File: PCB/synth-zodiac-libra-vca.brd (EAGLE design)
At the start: 160 x 100 mm, 29 parts, among them J4 6.35MM JACK, Q8 PNP, U2 LM13700

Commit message: Snapshot of designs so far.
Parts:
- removed C33: 2.2uF/16V, rlc:CAP_ALUM_SMT_4
- removed C34, C35: 0.1uF, rlc:0603-CAP
- removed J4: 6.35MM JACK, con-trs:TE-CK-6.35-29B
- removed JMP1, JMP2, JMP3, JMP4, JMP5, JMP6, JMP7: NP, rlc:0603-RES
- removed JMP62: 0, rlc:0603-RES
- removed R46, R48: 681R, rlc:0603-RES
- removed R47: 33.2K, rlc:0603-RES
- removed R49: 4.99K, rlc:0603-RES
- removed R50, R54, R55: 10.0K, rlc:0603-RES
- removed R51: 12.1K, rlc:0603-RES
- removed R52: 475R, rlc:0603-RES
- removed R53: 4.75M, rlc:0603-RES
- removed R56: 499K, rlc:0603-RES
- removed U2: LM13700, op-amp:SO16
- removed VCF_OUT: TPTHD-038, con-testpoints:THD-038MIL-X1
- added +, -, A.OUT, A_BIAS, BUF.I, BUF.O, D_BIAS: PADSMD-050X050, con-testpoints:SMD-050X050
- added AUD_OUT_TS, TP_COW_IN, TP_VCF_IN: TPSMD-040-RND, con-testpoints:SMD-040MIL-RND
- added A_OUT, COW_IN, EG_IN, VCF_IN: 2-pin, VT, SMT, con-jst:B2B-PH-SM4
- added C1: 2.2uF/16V, rlc:CAP_ALUM_SMT_4
- added C2, C3: 0.1uF, rlc:0603-CAP
- added CONST: Libra, circuit-monkey-zodiac:LIBRA-CONST
- added GLYPH: Libra, circuit-monkey-zodiac:LIBRA-GLYPH
- added J1: (no value), con-jst:B4B-PH-SM4
- added JMP8: NP, rlc:0603-SHORT
- added MODE: SPDT, switch-thd:SS-12-F45-PNL-SMT
- added OUT: 6.35MM JACK, con-trs:PNL-6.35-SMT-PADS
- added PCB: PCB FAB, circuit-monkey-zodiac:PENTAGON-40MM-RAD
- added R1, R10, R2, R3, R4: 10.0K, rlc:0603-RES
- added R11: 4.75M, rlc:0603-RES
- added R12: 4.99K, rlc:0603-RES
- added R13: 12.1K, rlc:0603-RES
- added R14: 475R, rlc:0603-RES
- added R5: 22.1K, rlc:0603-RES
- added R6: 499K, rlc:0603-RES
- added R7: 33.2K, rlc:0603-RES
- added R8, R9: 681R, rlc:0603-RES
- added U1: LM13700, op-amp:SO16
- AUD_OUT, TP1: value TPTHD-038 -> TPSMD-040-RND; device con-testpoints:THD-038MIL-X1 -> con-testpoints:SMD-040MIL-RND
- GND_VCA: value TPTHD-SCOPE-LOOP -> TPSMD-040-RND; device con-testpoints:TP-2P-THD -> con-testpoints:SMD-040MIL-RND
- moved TP1 111.3 mm to (33.4, 43.2), flipped to the bottom
- moved Q8 95.5 mm to (31.9, 47.5), flipped to the bottom, turned to 90 degrees
- moved GND_VCA 82.6 mm to (17.6, 41.6), flipped to the bottom, turned to 180 degrees
- moved AUD_OUT 79.3 mm to (23.7, 34.1), flipped to the bottom, turned to 180 degrees
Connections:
- removed net N$71: JMP5.1, U2.5
- removed net N$72: JMP2.2, U2.2
- removed net N$74: JMP6.2, U2.7
- removed net N$75: JMP7.1, U2.8
- new net AUDIO_OUT_TS: AUD_OUT_TS.TP, A_OUT.1, OUT.TS
- new net COWBELL_IN: COW_IN.1, R2.1, TP_COW_IN.TP
- new net EG_VCA: EG_IN.1, MODE.A
- new net N$1: D_BIAS.1, U1.2
- new net N$142: MODE.B, R5.1
- new net N$2: A.OUT.1, U1.5
- new net N$3: BUF.I.1, U1.7
- new net N$4: BUF.O.1, U1.8
- new net VCF_IN: R1.1, TP_VCF_IN.TP, VCF_IN.1
- net +9V: now also C2.2, J1.1, R5.2, U1.11; no longer C34.2, U2.11
- net -9V: now also C3.1, J1.2, R11.1, R13.1, R6.1, U1.6; no longer C35.1, R53.1, R56.1, U2.6
- net AUDIO_OUT: now also AUD_OUT.TP, OUT.T, R14.2; no longer AUD_OUT.1, J4.T, R52.2
- net EXP_VCA_CV: now also R4.1, R6.2; no longer R55.1, R56.2
- net GND: now also A_OUT.2, C2.1, C3.2, COW_IN.2, EG_IN.2, GND_VCA.TP, J1.4, MODE.MTG1, MODE.MTG2, OUT.S, OUT.SS, PCB.MTG1, PCB.MTG2, PCB.MTG3, PCB.MTG4, PCB.MTG5, R12.1, R8.1, R9.1, VCF_IN.2; no longer C34.1, C35.2, GND_VCA.1, GND_VCA.2, J4.S, R46.1, R48.1, R49.1, R51.1
- net N$45: now also R9.2, U1.13; no longer R46.2, U2.13
- net N$60: now also R7.2, R8.2, U1.14; no longer R47.2, R48.2, U2.14
- net N$61: now also TP1.TP, U1.15; no longer TP1.1, U2.15
- net N$62: now also R12.2, U1.10, U1.12; no longer R49.2, U2.10, U2.12
- net N$63: now also R10.2, U1.16; no longer R50.2, U2.16
- net N$64: now also C1.POS, R13.2, U1.9; no longer C33.POS, R51.2, U2.9
- net N$65: now also C1.NEG, R14.1; no longer C33.NEG, R52.1
- net N$66: now also R10.1, R11.2; no longer R50.1, R53.2
- net N$67: now also JMP8.4; no longer JMP62.2
- net N$68: now also JMP8.3, R3.2, R4.2; no longer JMP62.1, R54.2, R55.2
- net N$69: now also -.1, U1.4; no longer JMP1.2, U2.4
- net N$70: now also +.1, U1.3; no longer JMP3.2, U2.3
- net N$73: now also A_BIAS.1, U1.1; no longer JMP4.2, U2.1
- net VCA_CV: now also MODE.C, R3.1; no longer R54.1
- net VCF_OUT: now also R1.2, R2.2, R7.1; no longer R47.1, VCF_OUT.1
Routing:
- net +9V: track 0.00 -> 117.1 mm
- net -9V: track 0.00 -> 86.7 mm
- net COWBELL_IN: track 0.00 -> 41.0 mm
- net AUDIO_OUT: track 0.00 -> 32.7 mm
- net AUDIO_OUT_TS: track 0.00 -> 27.6 mm
- net EG_VCA: track 0.00 -> 25.2 mm
- net N$142: track 0.00 -> 20.8 mm
- net N$67: track 0.00 -> 17.8 mm
- net VCA_CV: track 0.00 -> 14.9 mm
- net N$66: track 0.00 -> 13.0 mm
- net N$64: track 0.00 -> 13.0 mm
- net VCF_OUT: track 0.00 -> 11.8 mm, vias 0 -> 2
- net VCF_IN: track 0.00 -> 11.3 mm
- net N$62: track 0.00 -> 10.6 mm, vias 0 -> 2
- net N$60: track 0.00 -> 6.85 mm
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- added copper zone on layer 1, net GND
- added copper zone on layer 16, net GND
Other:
- board size 160 x 100 mm -> 76.1 x 72.4 mm
- board text added: "L I B R A"
- board text added: "VCA"

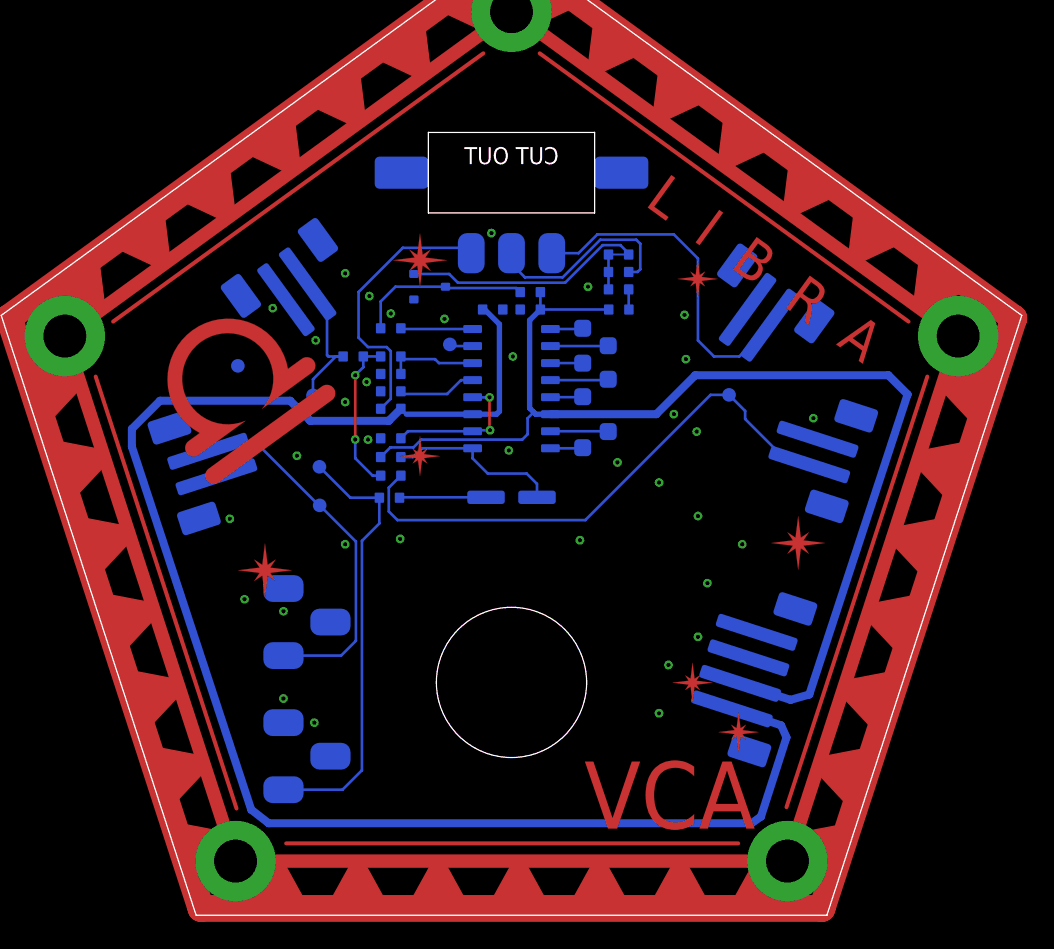
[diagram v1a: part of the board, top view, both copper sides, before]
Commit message: Almost ready for FAB.
Sagittarius was mis-spelled, renamed it.  Taurus is still WIP.
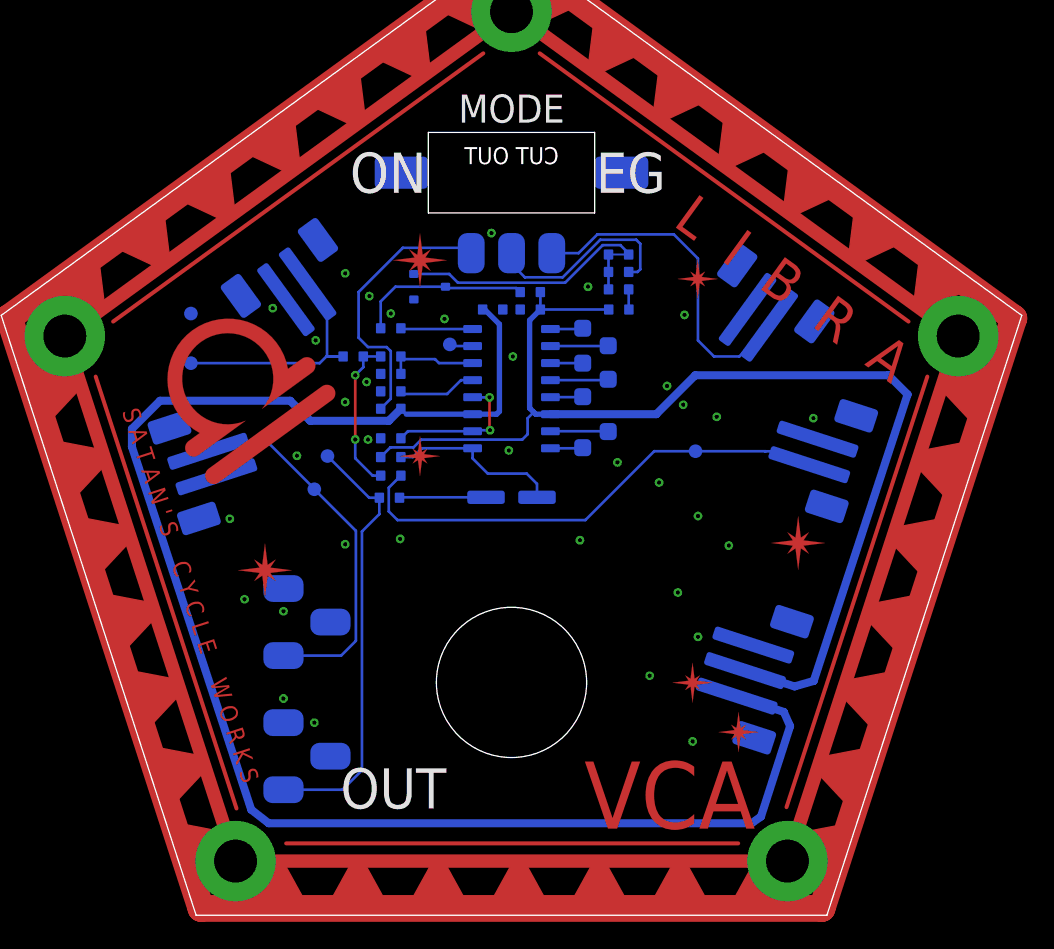
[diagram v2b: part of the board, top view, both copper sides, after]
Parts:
- removed AUD_OUT_TS, TP_COW_IN: TPSMD-040-RND, con-testpoints:SMD-040MIL-RND
- removed J1: (no value), con-jst:B4B-PH-SM4
- added AUD_OUT_TRS, TP_COW: TPSMD-040-RND, con-testpoints:SMD-040MIL-RND
- added PWR: JST, 3P, VT, SMT, con-jst:B3B-PH-SM4
- moved TP_VCF_IN 9.41 mm to (14.1, 41.8)
- moved GND_VCA 5.24 mm to (14.1, 45.5)
- moved AUD_OUT 1.00 mm to (24.3, 34.9)
- renumbered A_OUT to OUT2AMP, JMP8 to JMP1, Q8 to Q1
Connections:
- net +9V: now also PWR.1; no longer J1.1
- net -9V: now also PWR.2; no longer J1.2
- net AUDIO_OUT_TS: now also AUD_OUT_TRS.TP; no longer AUD_OUT_TS.TP
- net COWBELL_IN: now also TP_COW.TP; no longer TP_COW_IN.TP
- net GND: now also PWR.3; no longer J1.4
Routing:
- net VCF_IN: track 11.3 -> 18.8 mm
- net COWBELL_IN: track 41.0 -> 37.2 mm
- net -9V: track 86.7 -> 85.6 mm
- net +9V: track 117.1 -> 118.0 mm
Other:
- board text added: "EG"
- board text added: "ON"
- board text added: "OUT"
- board text added: "Rev. A"
- board text added: "S A T A N ' S C Y C L E W O R K S"

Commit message: Work in progress for rev A,  VCO rev.B
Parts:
- removed +, -, A.OUT, A_BIAS, BUF.I, BUF.O, D_BIAS: PADSMD-050X050, con-testpoints:SMD-050X050
- removed JMP1: NP, rlc:0603-SHORT
- removed R4: 10.0K, rlc:0603-RES
- removed R6: 499K, rlc:0603-RES
- COW_IN, EG_IN, OUT2AMP, VCF_IN: value 2-pin, VT, SMT -> JST, SH, 2P; device con-jst:B2B-PH-SM4 -> con-jst:BM02B-SRSS-TB
- MODE: value SPDT -> (none)
- PWR: value JST, 3P, VT, SMT -> JST SM 3P; device con-jst:B3B-PH-SM4 -> con-jst:BM03B-SRSS-TB
- moved R10 19.6 mm to (48.6, 45.6), turned to 0 degrees
- moved R13 18.5 mm to (47.3, 32.2), turned to 0 degrees
- moved Q1 17.6 mm to (48.6, 42.1), turned to 270 degrees
- moved GND_VCA 15.5 mm to (19.9, 31.1)
- moved TP_VCF_IN 12.4 mm to (25.7, 46.2)
- moved R11 9.59 mm to (48.6, 44.4), turned to 180 degrees
- moved R1 8.85 mm to (34.8, 44.4)
- moved AUD_OUT 7.94 mm to (30.7, 30.2)
- moved R14 5.90 mm to (34.8, 31.7)
- moved R2 5.81 mm to (34.8, 33.0)
- moved R5 5.81 mm to (34.8, 38.0)
- moved R7 5.81 mm to (34.8, 42.0)
- moved R8 5.81 mm to (34.8, 40.7)
- moved R9 5.81 mm to (34.8, 39.4)
- moved R12 5.80 mm to (34.8, 36.2)
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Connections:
- removed net EXP_VCA_CV: R4.1, R6.2
- removed net N$1: D_BIAS.1, U1.2
- removed net N$2: A.OUT.1, U1.5
- removed net N$3: BUF.I.1, U1.7
- removed net N$4: BUF.O.1, U1.8
- removed net N$67: JMP1.4, Q1.2
- removed net N$69: -.1, U1.4
- removed net N$70: +.1, U1.3
- removed net N$73: A_BIAS.1, U1.1
- net -9V: no longer R6.1
- net EG_VCA: now also MODE.B; no longer MODE.A
- net GND: now also U1.3, U1.4, U1.7
- net N$142: now also MODE.A; no longer MODE.B
- net N$68: now also Q1.2; no longer JMP1.3, R4.2
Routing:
- net +9V: track 118.0 -> 41.6 mm, vias 0 -> 2
- net -9V: track 85.6 -> 39.0 mm, vias 0 -> 2
- net N$67: track 17.8 -> 0.00 mm
- net N$142: track 20.8 -> 37.7 mm
- net N$66: track 13.0 -> 4.30 mm
- net VCA_CV: track 14.9 -> 22.8 mm
- net VCF_IN: track 18.8 -> 12.0 mm
- net N$63: track 5.37 -> 11.9 mm
- net COWBELL_IN: track 37.2 -> 31.0 mm
- net EG_VCA: track 25.2 -> 31.0 mm
- net N$68: track 2.60 -> 7.81 mm
- net N$69: track 4.33 -> 0.00 mm
- net N$3: track 4.32 -> 0.00 mm
- net N$1: track 4.32 -> 0.00 mm
- net AUDIO_OUT: track 32.5 -> 36.3 mm
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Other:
- board text removed: "EG"
- board text removed: "ON"

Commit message: Perhaps final Rev. A?
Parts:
- MODE: device switch-thd:SS-12-F45-PNL-SMT -> switch-thd:SS-12-F45-PNL-SMT-2
- moved MODE 2.00 mm to (38.0, 56.4), flipped to the top, turned to 0 degrees
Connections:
- net GND: now also MODE.MTG3, MODE.MTG4
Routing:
- net VCA_CV: track 22.8 -> 14.3 mm
- net N$142: track 37.7 -> 29.5 mm
- net EG_VCA: track 31.0 -> 32.6 mm
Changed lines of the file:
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@@
 <wire x1="54.15" y1="21.45" x2="53.65" y2="20.8" width="0.4" layer="42"/>
 <wire x1="54.15" y1="21.45" x2="53.65" y2="20.8" width="0.4" layer="30"/>
-<wire x1="45.3" y1="56.5" x2="45.3" y2="53" width="0.2" layer="21"/>
-<wire x1="45.3" y1="53" x2="49.9" y2="53" width="0.2" layer="21"/>
+<wire x1="43.2" y1="55.7" x2="43.2" y2="52.6" width="0.2" layer="21"/>
+<wire x1="43.2" y1="52.6" x2="48" y2="52.6" width="0.2" layer="21"/>
 <polygon width="0.1" layer="21">
-<vertex x="45.7" y="53.4"/>
-<vertex x="45.7" y="55.8"/>
-<vertex x="46.5" y="54.7"/>
-<vertex x="47.6" y="54.7"/>
-<vertex x="49.5" y="53.4"/>
+<vertex x="43.6" y="53"/>
+<vertex x="43.6" y="55.4"/>
+<vertex x="44.4" y="54.3"/>
+<vertex x="45.5" y="54.3"/>
+<vertex x="47.4" y="53"/>
 </polygon>
-<wire x1="26" y1="56.2" x2="26" y2="53.2" width="0.2" layer="21"/>
-<wire x1="26" y1="53.2" x2="31" y2="53.2" width="0.2" layer="21"/>
+<wire x1="28.5" y1="55.6" x2="28.5" y2="52.6" width="0.2" layer="21"/>
+<wire x1="28.5" y1="52.6" x2="33.5" y2="52.6" width="0.2" layer="21"/>
 <polygon width="0.1" layer="21">
-<vertex x="26.4" y="53.6"/>
-<vertex x="26.4" y="55.4"/>
-<vertex x="30.5" y="55.4"/>
-<vertex x="30.5" y="53.6"/>
+<vertex x="28.9" y="53"/>
+<vertex x="28.9" y="54.8"/>
+<vertex x="33" y="54.8"/>
+<vertex x="33" y="53"/>
 </polygon>
 <wire x1="29.7" y1="15.4" x2="22.8" y2="15.4" width="0.2" layer="21"/>
@@
 <attribute name="VALUE" x="15.21890625" y="30.012003125" size="0.4064" layer="28" font="vector" rot="MR252" align="center"/>
 </element>
-<element name="MODE" library="switch-thd" library_urn="urn:adsk.eagle:library:26242324" package="SS-12-F45-PNL-SMT" package3d_urn="urn:adsk.eagle:package:36475164/3" value="" x="38" y="54.4" smashed="yes" rot="MR180">
-<attribute name="COST01" value="0.15" x="38" y="54.4" size="1.778" layer="28" rot="MR180" display="off"/>
-<attribute name="COST10" value="0.12" x="38" y="54.4" size="1.778" layer="28" rot="MR180" display="off"/>
-<attribute name="COST100" value="0.12" x="38" y="54.4" size="1.778" layer="28" rot="MR180" display="off"/>
-<attribute name="MFR" value="Tayda" x="38" y="54.4" size="1.778" layer="28" rot="MR180" display="off"/>
-<attribute name="MPN" value="A-659 / A-5111" x="38" y="54.4" size="1.778" layer="28" rot="MR180" display="off"/>
-<attribute name="NAME" x="38" y="58.329" size="1" layer="25" align="bottom-center"/>
-<attribute name="NAME" x="38" y="50.971" size="1.27" layer="26" ratio="15" rot="MR180" align="bottom-center"/>
-<attribute name="VALUE" x="38" y="56.813" size="0.6096" layer="28" rot="MR180" align="bottom-center"/>
+<element name="MODE" library="switch-thd" library_urn="urn:adsk.eagle:library:26242324" package="SS-12-F45-PNL-SMT-2" value="" x="38" y="56.4" smashed="yes">
+<attribute name="COST01" value="0.15" x="38" y="56.4" size="1.778" layer="27" display="off"/>
+<attribute name="COST10" value="0.12" x="38" y="56.4" size="1.778" layer="27" display="off"/>
+<attribute name="COST100" value="0.12" x="38" y="56.4" size="1.778" layer="27" display="off"/>
+<attribute name="MFR" value="Tayda" x="38" y="56.4" size="1.778" layer="27" display="off"/>
+<attribute name="MPN" value="A-659/A-5111/A-5104" x="38" y="56.4" size="1.778" layer="27" display="off"/>
+<attribute name="NAME" x="38" y="52.471" size="1" layer="26" rot="MR180" align="bottom-center"/>
+<attribute name="NAME" x="38" y="59.829" size="1.27" layer="25" ratio="15" align="bottom-center"/>
+<attribute name="VALUE" x="38" y="53.987" size="0.6096" layer="27" align="bottom-center"/>
 </element>
 </elements>
@@
 <via x="26.9" y="50.5" extent="1-16" drill="0.3048"/>
 <via x="42.1" y="50" extent="1-16" drill="0.3048"/>
-<via x="47.2" y="49.8" extent="1-16" drill="0.3048"/>
+<via x="47.8" y="50.9" extent="1-16" drill="0.3048"/>
 <via x="49" y="40.2" extent="1-16" drill="0.3048"/>
 <via x="53.3" y="37.8" extent="1-16" drill="0.3048"/>
@@
 <contactref element="MODE" pad="MTG2"/>
 <via x="52.7" y="22.7" extent="1-16" drill="0.3048"/>
+<contactref element="MODE" pad="MTG4"/>
+<contactref element="MODE" pad="MTG3"/>
+<via x="28.7" y="47.7" extent="1-16" drill="0.3048"/>
 </signal>
 <signal name="+9V">
@@
 <contactref element="R3" pad="1"/>
 <contactref element="MODE" pad="C"/>
-<wire x1="48.29533125" y1="49.19533125" x2="48.7" y2="49.6" width="0.2" layer="16"/>
 <wire x1="47.832159375" y1="47" x2="48.29533125" y2="47.463171875" width="0.2" layer="16"/>
-<wire x1="48.29533125" y1="49.19533125" x2="48.29533125" y2="47.463171875" width="0.2" layer="16"/>
-<wire x1="39.208175" y1="58.591825" x2="38" y2="59.8" width="0.2" layer="16"/>
-<wire x1="38" y1="59.8" x2="38" y2="60.4" width="0.2" layer="16"/>
-<wire x1="48.7" y1="49.6" x2="48.7" y2="57.1604875" width="0.2" layer="16"/>
-<wire x1="48.7" y1="57.1604875" x2="46.691965625" y2="58.581540625" width="0.2" layer="16"/>
-<wire x1="46.691965625" y1="58.581540625" x2="39.208175" y2="58.591825" width="0.2" layer="16"/>
+<wire x1="48.29533125" y1="48.90466875" x2="48.29533125" y2="47.463171875" width="0.2" layer="16"/>
+<wire x1="38" y1="51.3" x2="38.1" y2="51.2" width="0.2" layer="16"/>
+<wire x1="38.1" y1="51.2" x2="38.1" y2="50.7" width="0.2" layer="16"/>
+<wire x1="38.1" y1="50.7" x2="38.9" y2="49.9" width="0.2" layer="16"/>
+<wire x1="46.5" y1="50.7" x2="48.29533125" y2="48.90466875" width="0.2" layer="16"/>
+<wire x1="38.9" y1="49.9" x2="40.7" y2="49.9" width="0.2" layer="16"/>
+<wire x1="40.7" y1="49.9" x2="41.5" y2="50.7" width="0.2" layer="16"/>
+<wire x1="41.5" y1="50.7" x2="46.5" y2="50.7" width="0.2" layer="16"/>
 </signal>
 <signal name="N$65">
@@
 <contactref element="EG_IN" pad="1"/>
 <contactref element="MODE" pad="B"/>
-<wire x1="46.863475" y1="59" x2="41.9" y2="59" width="0.2" layer="16"/>
-<wire x1="41.9" y1="59" x2="41" y2="59.9" width="0.2" layer="16"/>
-<wire x1="41" y1="60.4" x2="41" y2="59.9" width="0.2" layer="16"/>
-<wire x1="60.028175" y1="42.9634" x2="61.65755625" y2="44.59278125" width="0.2" layer="16"/>
-<wire x1="61.65755625" y1="48.327821875" x2="61.65755625" y2="44.59278125" width="0.2" layer="16"/>
-<wire x1="46.863475" y1="59" x2="61.65755625" y2="48.327821875" width="0.2" layer="16"/>
+<wire x1="60.028175" y1="42.9634" x2="61.70721875" y2="45.25755625" width="0.2" layer="16"/>
+<wire x1="61.65755625" y1="48.495421875" x2="61.70721875" y2="45.25755625" width="0.2" layer="16"/>
+<wire x1="52.086228125" y1="55.4" x2="61.65755625" y2="48.495421875" width="0.2" layer="16"/>
+<wire x1="47.9" y1="52.7" x2="47.9" y2="54.3" width="0.2" layer="16"/>
+<wire x1="47.9" y1="54.3" x2="49" y2="55.4" width="0.2" layer="16"/>
+<wire x1="49" y1="55.4" x2="52.086228125" y2="55.4" width="0.2" layer="16"/>
+<wire x1="40.2" y1="51.3" x2="40.4" y2="51.1" width="0.2" layer="16"/>
+<wire x1="46.3" y1="51.1" x2="40.4" y2="51.1" width="0.2" layer="16"/>
+<wire x1="46.3" y1="51.1" x2="47.9" y2="52.7" width="0.2" layer="16"/>
 </signal>
 <signal name="N$142">
@@
 <wire x1="36.3" y1="44" x2="34.8037625" y2="42.5037625" width="0.2" layer="16"/>
 <contactref element="MODE" pad="A"/>
-<wire x1="35" y1="60.4" x2="33.4" y2="58.8" width="0.2" layer="16"/>
-<wire x1="29.291690625" y1="58.8" x2="25.9" y2="56.342253125" width="0.2" layer="16"/>
-<wire x1="25.9" y1="56.342253125" x2="25.9" y2="49.2" width="0.2" layer="16"/>
-<wire x1="25.9" y1="49.2" x2="28.8" y2="46.3" width="0.2" layer="16"/>
+<wire x1="28.6" y1="46.3" x2="27.5" y2="47.4" width="0.2" layer="16"/>
 <wire x1="36.27104375" y1="44.8" x2="36.3" y2="44.8" width="0.2" layer="16"/>
 <wire x1="34.819" y1="45.081" x2="35.99004375" y2="45.081" width="0.2" layer="16"/>
 <wire x1="35.99004375" y1="45.081" x2="36.27104375" y2="44.8" width="0.2" layer="16"/>
-<wire x1="33.4" y1="58.8" x2="29.291690625" y2="58.8" width="0.2" layer="16"/>
-<wire x1="28.8" y1="46.3" x2="33.6" y2="46.3" width="0.2" layer="16"/>
+<wire x1="28.6" y1="46.3" x2="33.6" y2="46.3" width="0.2" layer="16"/>
 <wire x1="33.6" y1="46.3" x2="34.819" y2="45.081" width="0.2" layer="16"/>
+<wire x1="27.5" y1="47.4" x2="27.5" y2="49.7" width="0.2" layer="16"/>
+<wire x1="27.5" y1="49.7" x2="29.9" y2="52.1" width="0.2" layer="16"/>
+<wire x1="29.9" y1="52.1" x2="32.6" y2="52.1" width="0.2" layer="16"/>
+<wire x1="33.4" y1="51.3" x2="35.8" y2="51.3" width="0.2" layer="16"/>
+<wire x1="32.6" y1="52.1" x2="33.4" y2="51.3" width="0.2" layer="16"/>
 </signal>
 <signal name="AUDIO_OUT_TS">
